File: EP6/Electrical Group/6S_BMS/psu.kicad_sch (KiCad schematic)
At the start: 13 parts, among them Q13 2N7002, Q14 AO3401A, U6 78L05G-AB3-R, U7 HT7533

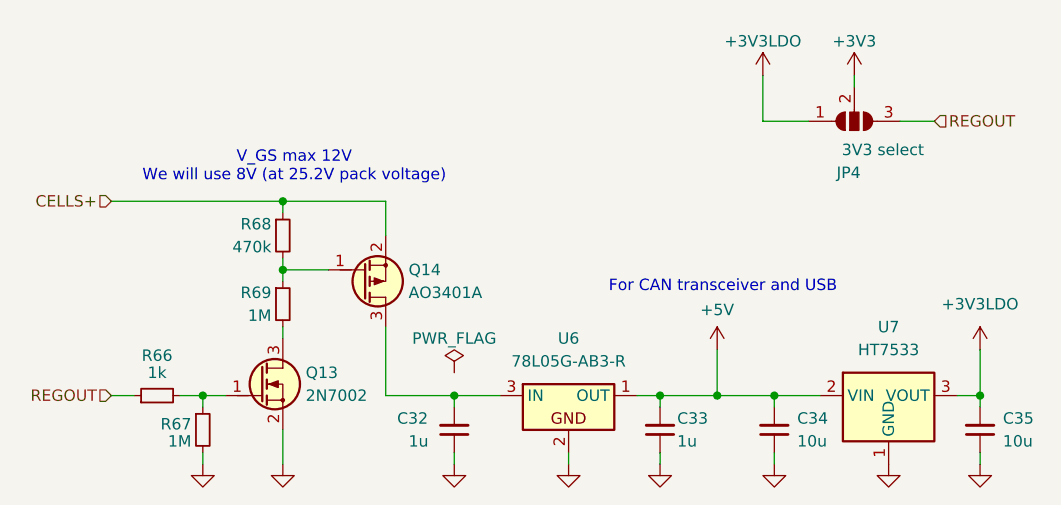
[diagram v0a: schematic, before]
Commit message: fix net ties and net classes
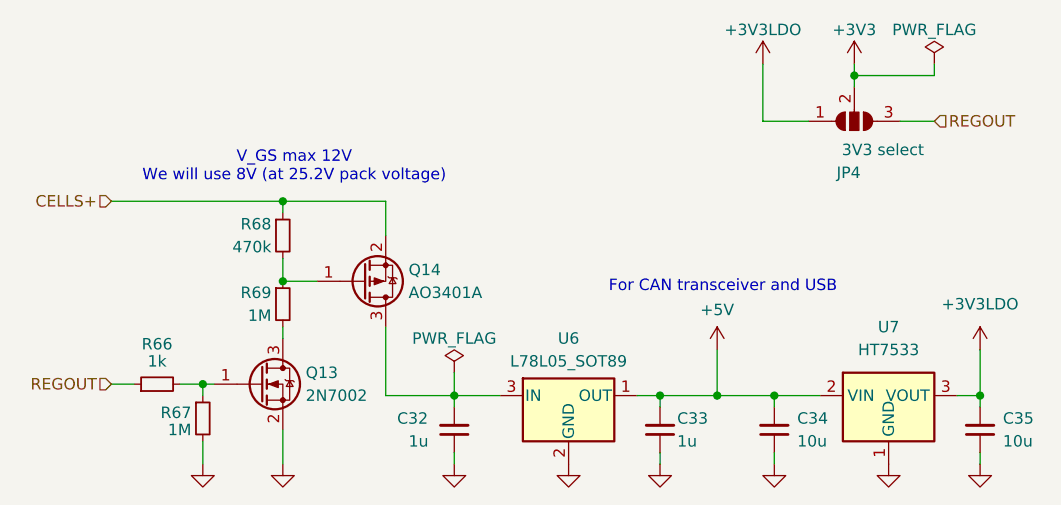
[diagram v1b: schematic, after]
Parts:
- removed Q13: 2N7002, Package_TO_SOT_SMD:SOT-23, symbol PCM_Transistor_MOSFET_AKL:2N7002
- removed Q14: AO3401A, Package_TO_SOT_SMD:SOT-23, symbol PCM_Transistor_MOSFET_AKL:AO3401A
- removed U6: 78L05G-AB3-R, Package_TO_SOT_SMD:SOT-89-3, symbol PCM_Voltage_Regulator_AKL:L78L05ABU
- added Q13: 2N7002, Package_TO_SOT_SMD:SOT-23, symbol Transistor_FET:2N7002
- added Q14: AO3401A, Package_TO_SOT_SMD:SOT-23, symbol Transistor_FET:AO3401A
- added U6: L78L05_SOT89, Package_TO_SOT_SMD:SOT-89-3, symbol Regulator_Linear:L78L05_SOT89
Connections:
- net +5V: now also U6.1 (OUT)
- net CELLS+: now also Q14.2 (S)
- net GND: now also Q13.2 (S), U6.2 (GND)
- net at R68.2, R69.1: now also Q14.1 (G)
- net at C32.2: now also Q14.3 (D), U6.3 (IN)
- net at R69.2: now also Q13.3 (D)
- net at R66.2, R67.1: now also Q13.1 (G)
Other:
- moved on the sheet: R66, R67

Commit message: Board kinda done
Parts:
- removed JP4: 3V3 select, Jumper:SolderJumper-3_P1.3mm_Open_Pad1.0x1.5mm, symbol Jumper:SolderJumper_3_Open
- removed U7: HT7533, Package_TO_SOT_SMD:SOT-89-3, symbol Regulator_Linear:HT75xx-1-SOT89
- added JP4: 3V3_LDO, Jumper:SolderJumper-2_P1.3mm_Open_TrianglePad1.0x1.5mm, symbol Jumper:SolderJumper_2_Open
- added U8: XC6206PxxxMR, Package_TO_SOT_SMD:SOT-23-3, symbol Regulator_Linear:XC6206PxxxMR
- C36: renamed from C34; value 10u -> 1u; footprint Capacitor_SMD:C_0603_1608Metric -> Capacitor_SMD:C_0402_1005Metric
- C37: renamed from C35; value 10u -> 1u
- renumbered C32 to C34, C33 to C35, U6 to U7
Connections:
- net +3V3: now also JP4.1 (A)
- net +3V3LDO: now also JP4.2 (B), U8.2 (VO)
- net +5V: now also U8.3 (VI)
- net GND: now also U8.1 (GND)
